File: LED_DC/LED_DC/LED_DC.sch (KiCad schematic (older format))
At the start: 0 parts

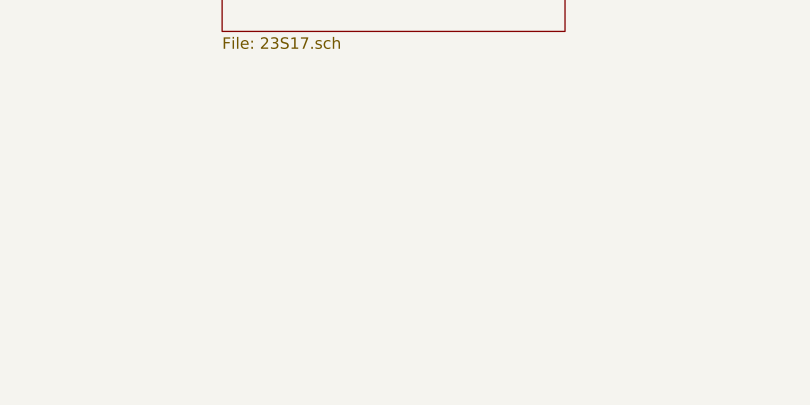
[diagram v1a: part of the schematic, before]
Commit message: Added keypad connector.
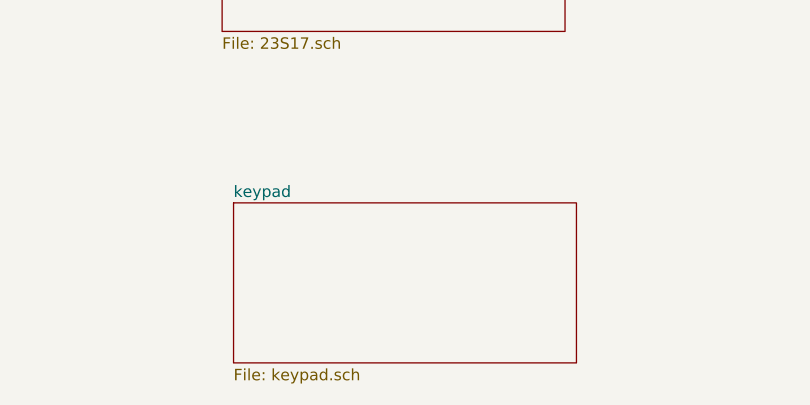
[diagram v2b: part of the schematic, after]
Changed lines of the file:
@@
 $Descr A4 11693 8268
 encoding utf-8
-Sheet 1 4
+Sheet 1 5
 Title ""
 Date ""
@@
 F1 "SevenSegment.sch" 50
 $EndSheet
+$Sheet
+S 3800 3350 1500 700
+U 5FEBB696
+F0 "keypad" 50
+F1 "keypad.sch" 50
+$EndSheet
 $EndSCHEMATC
